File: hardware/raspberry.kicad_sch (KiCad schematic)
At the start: 30 parts, among them J3 Conn_01x04, U1 RP2040, U2 W25Q128JVS, Y1 Crystal_GND24

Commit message: saved changes
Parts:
- renumbered TP16 to TP10, TP19 to TP11, TP20 to TP12, TP1 to TP2, TP2 to TP3, TP6 to TP5, TP8 to TP6, TP10 to TP7, TP12 to TP8, TP14 to TP9
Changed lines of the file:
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@@
 		(on_board yes)
 		(dnp no)
-		(property "Reference" "TP8"
+		(property "Reference" "TP6"
 			(at 197.104 73.66 90)
 			(effects
@@
 			(project "flute"
 				(path "/9ae53f79-8ce2-4a44-ba8e-dca375125c34/739c4558-e5ce-473d-85db-8208f7847074"
-					(reference "TP8")
+					(reference "TP6")
 					(unit 1)
 				)
@@
 		(on_board yes)
 		(dnp no)
-		(property "Reference" "TP12"
+		(property "Reference" "TP8"
 			(at 196.85 101.6 90)
 			(effects
@@
 			(project "flute"
 				(path "/9ae53f79-8ce2-4a44-ba8e-dca375125c34/739c4558-e5ce-473d-85db-8208f7847074"
-					(reference "TP12")
+					(reference "TP8")
 					(unit 1)
 				)
@@
 		(on_board yes)
 		(dnp no)
-		(property "Reference" "TP14"
+		(property "Reference" "TP9"
 			(at 196.85 106.68 90)
 			(effects
@@
 			(project "flute"
 				(path "/9ae53f79-8ce2-4a44-ba8e-dca375125c34/739c4558-e5ce-473d-85db-8208f7847074"
-					(reference "TP14")
+					(reference "TP9")
 					(unit 1)
 				)
@@
 		(on_board yes)
 		(dnp no)
-		(property "Reference" "TP20"
+		(property "Reference" "TP12"
 			(at 196.85 127 90)
 			(effects
@@
 			(project "flute"
 				(path "/9ae53f79-8ce2-4a44-ba8e-dca375125c34/739c4558-e5ce-473d-85db-8208f7847074"
-					(reference "TP20")
+					(reference "TP12")
 					(unit 1)
 				)
@@
 		(on_board yes)
 		(dnp no)
-		(property "Reference" "TP2"
+		(property "Reference" "TP3"
 			(at 100.33 60.96 90)
 			(effects
@@
 			(project "flute"
 				(path "/9ae53f79-8ce2-4a44-ba8e-dca375125c34/739c4558-e5ce-473d-85db-8208f7847074"
-					(reference "TP2")
+					(reference "TP3")
 					(unit 1)
 				)
@@
 		(on_board yes)
 		(dnp no)
-		(property "Reference" "TP10"
+		(property "Reference" "TP7"
 			(at 196.85 96.774 90)
 			(effects
@@
 			(project "flute"
 				(path "/9ae53f79-8ce2-4a44-ba8e-dca375125c34/739c4558-e5ce-473d-85db-8208f7847074"
-					(reference "TP10")
+					(reference "TP7")
 					(unit 1)
 				)
@@
 		(on_board yes)
 		(dnp no)
-		(property "Reference" "TP1"
+		(property "Reference" "TP2"
 			(at 196.85 52.0699 90)
 			(effects
@@
 			(project ""
 				(path "/9ae53f79-8ce2-4a44-ba8e-dca375125c34/739c4558-e5ce-473d-85db-8208f7847074"
-					(reference "TP1")
+					(reference "TP2")
 					(unit 1)
 				)
@@
 		(on_board yes)
 		(dnp no)
-		(property "Reference" "TP16"
+		(property "Reference" "TP10"
 			(at 196.85 111.76 90)
 			(effects
@@
 			(project "flute"
 				(path "/9ae53f79-8ce2-4a44-ba8e-dca375125c34/739c4558-e5ce-473d-85db-8208f7847074"
-					(reference "TP16")
+					(reference "TP10")
 					(unit 1)
 				)
@@
 		(on_board yes)
 		(dnp no)
-		(property "Reference" "TP6"
+		(property "Reference" "TP5"
 			(at 197.104 66.04 90)
 			(effects
@@
 			(project "flute"
 				(path "/9ae53f79-8ce2-4a44-ba8e-dca375125c34/739c4558-e5ce-473d-85db-8208f7847074"
-					(reference "TP6")
+					(reference "TP5")
 					(unit 1)
 				)
@@
 		(on_board yes)
 		(dnp no)
-		(property "Reference" "TP19"
+		(property "Reference" "TP11"
 			(at 196.85 124.46 90)
 			(effects
@@
 			(project "flute"
 				(path "/9ae53f79-8ce2-4a44-ba8e-dca375125c34/739c4558-e5ce-473d-85db-8208f7847074"
-					(reference "TP19")
+					(reference "TP11")
 					(unit 1)
 				)

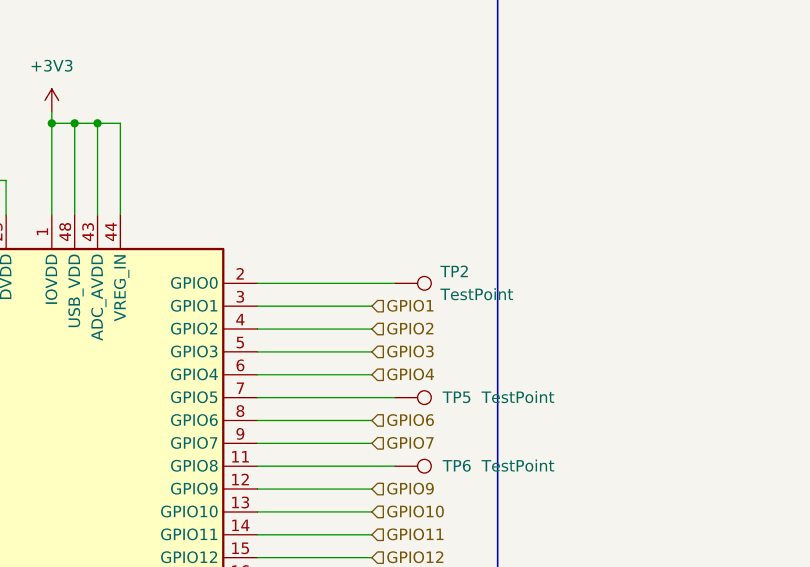
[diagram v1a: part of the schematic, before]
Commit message: problem with soldermask corrected
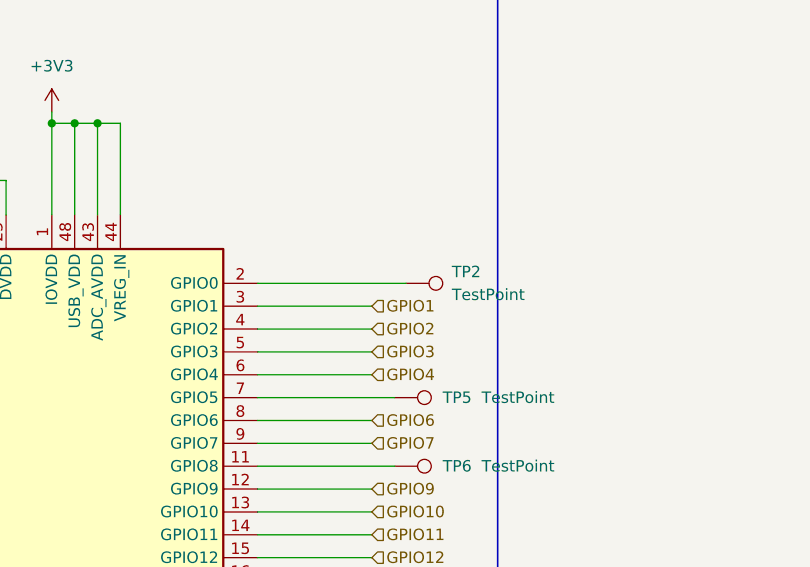
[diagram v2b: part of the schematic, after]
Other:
- moved on the sheet: TP2
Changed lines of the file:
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@@
 	(wire
 		(pts
-			(xy 176.53 53.34) (xy 191.77 53.34)
+			(xy 176.53 53.34) (xy 193.04 53.34)
 		)
 		(stroke
@@
 	(symbol
 		(lib_id "Connector:TestPoint")
-		(at 191.77 53.34 270)
+		(at 193.04 53.34 270)
 		(unit 1)
 		(exclude_from_sim no)
@@
 		(dnp no)
 		(property "Reference" "TP2"
-			(at 196.85 52.0699 90)
+			(at 198.12 52.0699 90)
 			(effects
 				(font
@@
 		)
 		(property "Value" "TestPoint"
-			(at 196.85 54.6099 90)
+			(at 198.12 54.6099 90)
 			(effects
 				(font
@@
 		)
 		(property "Footprint" "TestPoint:TestPoint_Pad_D1.5mm"
-			(at 191.77 58.42 0)
+			(at 193.04 58.42 0)
 			(effects
 				(font
@@
 		)
 		(property "Datasheet" "~"
-			(at 191.77 58.42 0)
+			(at 193.04 58.42 0)
 			(effects
 				(font
@@
 		)
 		(property "Description" "test point"
-			(at 191.77 53.34 0)
+			(at 193.04 53.34 0)
 			(effects
 				(font

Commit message: pcb ver1.1
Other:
- title: MINIMALISED RASBERRY PI PICO -> ELECTRONIC FLUTE
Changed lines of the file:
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@@
 	(paper "A4")
 	(title_block
-		(title "MINIMALISED RASBERRY PI PICO")
-		(date "2025-11-16")
+		(title "ELECTRONIC FLUTE")
+		(date "2025-12-02")
 		(rev "1.0")
 		(company "KN HARDWIRE AGH")
